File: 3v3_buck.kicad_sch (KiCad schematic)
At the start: 11 parts, among them U5 LMR51430

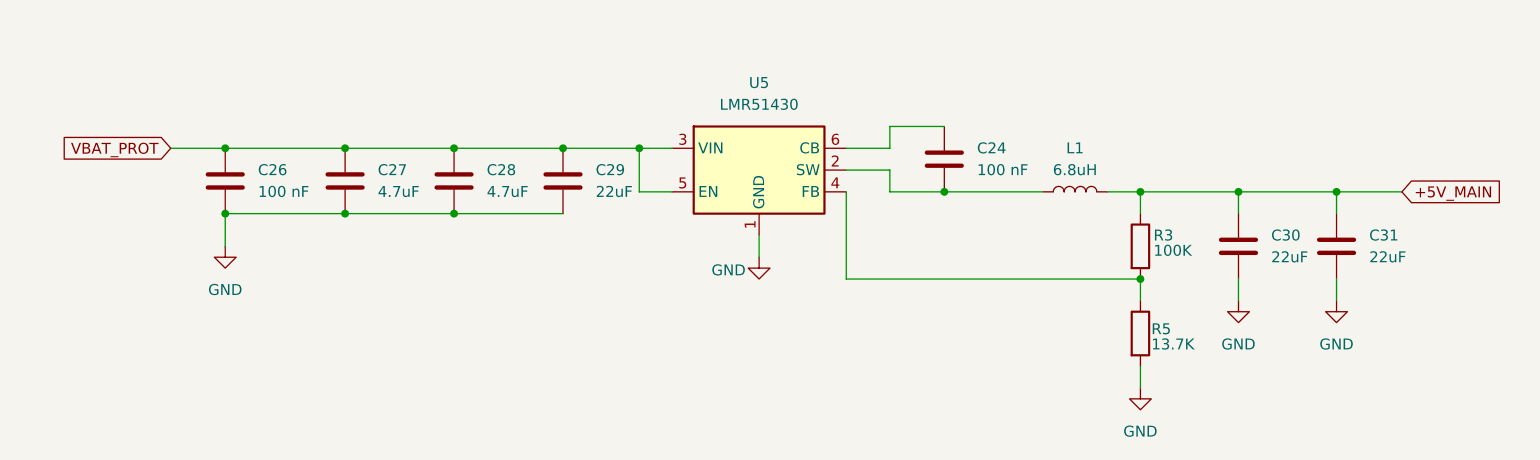
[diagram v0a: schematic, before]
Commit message: added 3v3 buck converter
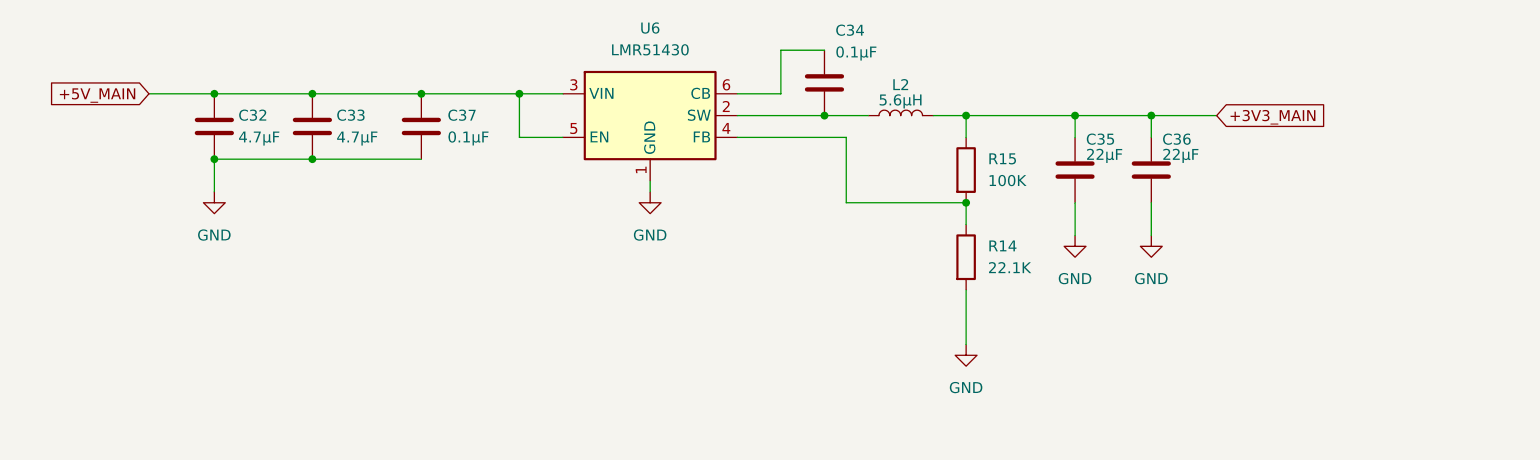
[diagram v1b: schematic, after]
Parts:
- removed C24, C26: 100 nF, symbol Device:C
- removed C27, C28: 4.7uF, symbol Device:C
- removed C29, C30, C31: 22uF, symbol Device:C
- removed L1: 6.8uH, symbol Device:L
- removed R3: 100K, symbol Device:R
- removed R5: 13.7K, symbol Device:R
- removed U5: LMR51430, Package_TO_SOT_SMD:SOT-23-6, symbol Regulator_Switching:LMR51430
- added C32, C33: 4.7µF, symbol Device:C
- added C34, C37: 0.1µF, symbol Device:C
- added C35, C36: 22µF, symbol Device:C
- added L2: 5.6µH, symbol Device:L
- added R14: 22.1K, symbol Device:R
- added R15: 100K, symbol Device:R
- added U6: LMR51430, Package_TO_SOT_SMD:SOT-23-6, symbol Regulator_Switching:LMR51430
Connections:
- net +5V_MAIN: now also C32.1, C33.1, C37.1, U6.3 (VIN), U6.5 (EN)
- net GND: now also C32.2, C33.2, C35.2, C36.2, C37.2, R14.2, U6.1 (GND)
- new net: R14.1, R15.2, U6.4 (FB)
- new net: C34.1, U6.6 (CB)
- new net: C34.2, L2.1, U6.2 (SW)
- new net +3V3_MAIN: C35.1, C36.1, L2.2, R15.1

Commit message: added for 3v3 and 5v capacitors, resistors and induction footprints
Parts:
- C32, C33: footprint (none) -> C3216X7R1H475M160AC:CAPC3216X180N
- C34, C37: footprint (none) -> C1608X7R1H474K080AC:CAPC1608X90N
- C35, C36: footprint (none) -> C1206C105K5RACAUTO:CAPC3216X178N
- L2: footprint (none) -> Inductor_SMD:L_Coilcraft_XAL6060-XXX
- R14, R15: footprint (none) -> Resistor_SMD:R_0201_0603Metric
- U6: value LMR51430 -> LMR51430_3v3
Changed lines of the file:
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@@
 			)
 		)
-		(property "Footprint" ""
+		(property "Footprint" "Resistor_SMD:R_0201_0603Metric"
 			(at 158.242 104.14 90)
 			(hide yes)
@@
 			)
 		)
-		(property "Footprint" ""
+		(property "Footprint" "C1608X7R1H474K080AC:CAPC1608X90N"
 			(at 144.4752 87.63 0)
 			(hide yes)
@@
 			)
 		)
-		(property "Footprint" ""
+		(property "Footprint" "C1608X7R1H474K080AC:CAPC1608X90N"
 			(at 97.4852 92.71 0)
 			(hide yes)
@@
 			)
 		)
-		(property "Footprint" ""
+		(property "Footprint" "C1206C105K5RACAUTO:CAPC3216X178N"
 			(at 182.5752 97.79 0)
 			(hide yes)
@@
 			)
 		)
-		(property "Footprint" ""
+		(property "Footprint" "C3216X7R1H475M160AC:CAPC3216X180N"
 			(at 73.3552 92.71 0)
 			(hide yes)
@@
 			)
 		)
-		(property "Footprint" ""
+		(property "Footprint" "Resistor_SMD:R_0201_0603Metric"
 			(at 158.242 93.98 90)
 			(hide yes)
@@
 			)
 		)
-		(property "Footprint" ""
+		(property "Footprint" "Inductor_SMD:L_Coilcraft_XAL6060-XXX"
 			(at 152.4 87.63 0)
 			(hide yes)
@@
 			)
 		)
-		(property "Footprint" ""
+		(property "Footprint" "C3216X7R1H475M160AC:CAPC3216X180N"
 			(at 84.7852 92.71 0)
 			(hide yes)
@@
 			)
 		)
-		(property "Value" "LMR51430"
+		(property "Value" "LMR51430_3v3"
 			(at 123.19 80.01 0)
 			(show_name no)
@@
 			)
 		)
-		(property "Footprint" ""
+		(property "Footprint" "C1206C105K5RACAUTO:CAPC3216X178N"
 			(at 173.6852 97.79 0)
 			(hide yes)

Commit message: change vbat_prot footprint and added pwrmux for 3v3 ubs_mcu connector
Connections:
- net +5V_MAIN renamed +VBAT_MUX
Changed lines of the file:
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@@
 		)
 	)
-	(global_label "+5V_MAIN"
+	(global_label "+VBAT_MUX"
 		(shape input)
 		(at 64.77 85.09 180)
@@
 		)
 		(property "Intersheetrefs" "${INTERSHEET_REFS}"
-			(at 52.4714 85.09 0)
+			(at 50.8386 85.09 0)
 			(hide yes)
 			(show_name no)
